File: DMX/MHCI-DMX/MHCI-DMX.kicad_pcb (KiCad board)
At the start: 2 copper layers, 100 x 100 mm, 36 parts, among them J1 XLR_Male, J2 XLR5_Female, J4 Barrel_Jack, K2 G5V-2, U2 TJA1051T, U4 74LVC1G08

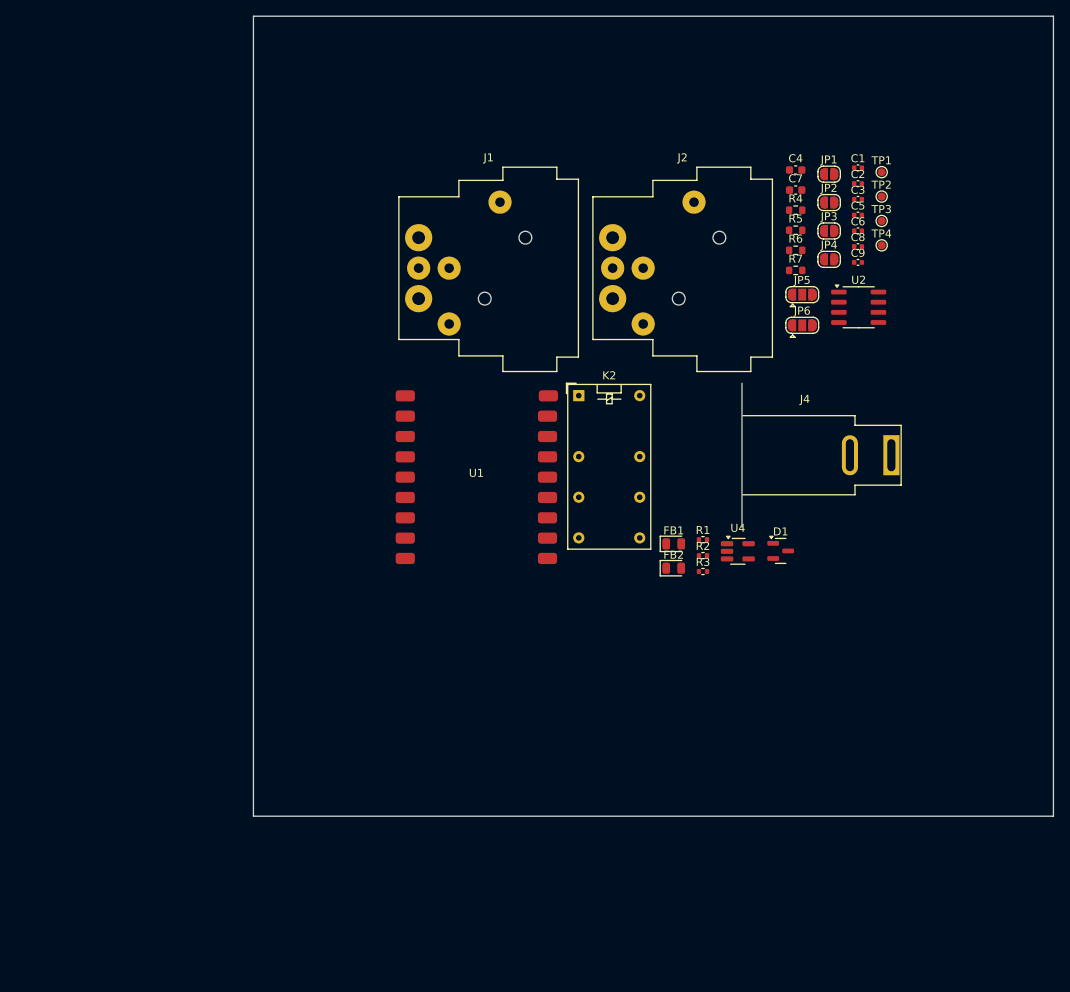
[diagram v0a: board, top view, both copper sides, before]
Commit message: DMX Schematic complete, and initial Layout
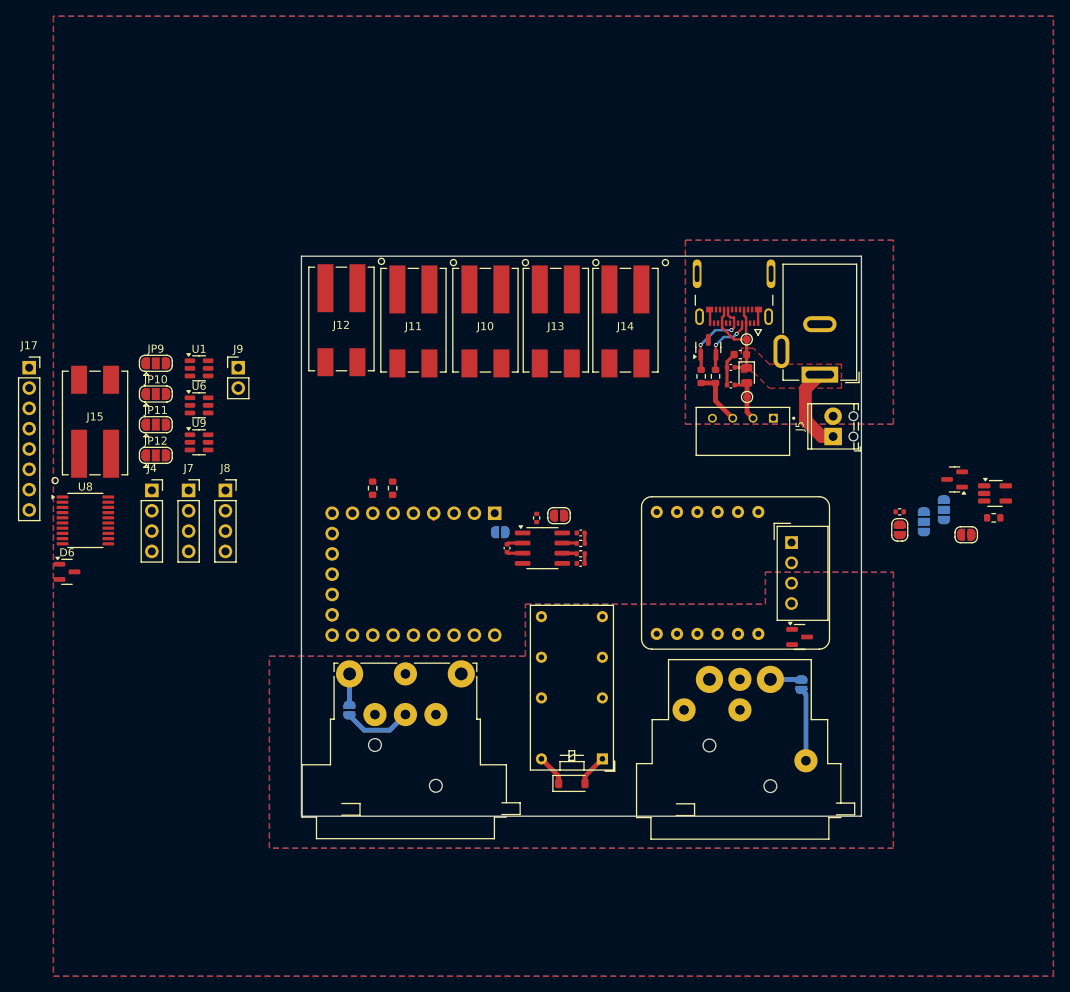
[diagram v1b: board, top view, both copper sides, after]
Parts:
- removed C7: 10uF, Capacitor_SMD:C_0603_1608Metric
- removed C8: 1uF, Capacitor_SMD:C_0402_1005Metric
- removed C9: 100nF, Capacitor_SMD:C_0402_1005Metric
- removed FB2: FerriteBead, Diode_SMD:D_0805_2012Metric
- removed TP3: VIN, TestPoint:TestPoint_Pad_D1.0mm
- removed TP4: 5V, TestPoint:TestPoint_Pad_D1.0mm
- added D2: D_TVS_Dual_AAC, Package_TO_SOT_SMD:SOT-23, F.Cu at (106.9, 91.4)
- added D4: D_TVS_Dual_AAC, Package_TO_SOT_SMD:SOT-23, F.Cu at (118.3, 127.6)
- added D6: D_TVS_Dual_AAC, Package_TO_SOT_SMD:SOT-23, F.Cu at (26.7, 119.5)
- added J10: Conn_01x02, MHCI:2060-452-998-404 Wago, F.Cu at (79.0, 88.0)
- added J11: Conn_01x02, MHCI:2060-452-998-404 Wago, F.Cu at (70.0, 88.0)
- added J12: Conn_01x02, MHCI:2060-452-998-404 Wago, F.Cu at (61.0, 87.8)
- added J13: Conn_01x02, MHCI:2060-452-998-404 Wago, F.Cu at (87.8, 88.0)
- added J14: Conn_01x02, MHCI:2060-452-998-404 Wago, F.Cu at (96.5, 88.0)
- added J15: Conn_01x02, MHCI:2060-452-998-404 Wago, F.Cu at (30.2, 100.9)
- added J17: Conn_01x08, Connector_PinSocket_2.54mm:PinSocket_1x08_P2.54mm_Vertical, F.Cu at (22.0, 93.9)
- added J3: 2012670005, LandingLight:MOLEX_2012670005, F.Cu at (110.1, 80.4)
- added J5: Conn_01x02, TerminalBlock_Phoenix:TerminalBlock_Phoenix_MPT-0,5-2-2.54_1x02_P2.54mm_Horizontal, F.Cu at (122.5, 102.5)
- added J6: Barrel_Jack_MountingPin, Connector_BarrelJack:BarrelJack_GCT_DCJ200-10-A_Horizontal, F.Cu at (120.8, 94.8)
- added J7: Conn_01x04, Connector_PinSocket_2.54mm:PinSocket_1x04_P2.54mm_Vertical, F.Cu at (41.9, 109.3)
- added J8: Conn_01x04, Connector_PinSocket_2.54mm:PinSocket_1x04_P2.54mm_Vertical, F.Cu at (46.5, 109.3)
- added J9: Conn_01x02, Connector_PinHeader_2.54mm:PinHeader_1x02_P2.54mm_Vertical, F.Cu at (48.1, 93.9)
- added JP10: SolderJumper_3_Open, Jumper:SolderJumper-3_P1.3mm_Open_RoundedPad1.0x1.5mm, F.Cu at (37.8, 97.2)
- added JP11: SolderJumper_3_Open, Jumper:SolderJumper-3_P1.3mm_Open_RoundedPad1.0x1.5mm, F.Cu at (37.8, 101.1)
- added JP12: SolderJumper_3_Open, Jumper:SolderJumper-3_P1.3mm_Open_RoundedPad1.0x1.5mm, F.Cu at (37.8, 104.9)
- added JP7: Jumper_2_Open, Jumper:SolderJumper-2_P1.3mm_Open_RoundedPad1.0x1.5mm, F.Cu at (139.1, 114.8)
- added JP8: Jumper_2_Open, Jumper:SolderJumper-2_P1.3mm_Open_RoundedPad1.0x1.5mm, F.Cu at (130.8, 114.2)
- added JP9: SolderJumper_3_Open, Jumper:SolderJumper-3_P1.3mm_Open_RoundedPad1.0x1.5mm, F.Cu at (37.8, 93.4)
- added PS1: TBA1-0510, MHCI:CONV_TBA1-0510, F.Cu at (111.2, 101.9)
- added Q1: PMOS, Package_TO_SOT_SMD:SOT-23, F.Cu at (137.6, 107.9)
- added R8: 100k, Resistor_SMD:R_0603_1608Metric, F.Cu at (142.5, 112.7)
- added R9: 120R, Resistor_SMD:R_0402_1005Metric, F.Cu at (130.8, 112.0)
- added U3: ~, MHCI:ISO-DMX, F.Cu at (113.1, 119.6)
- added U5: TME-0505S, Converter_DCDC:Converter_DCDC_TRACO_TME_03xxS_05xxS_12xxS_Single_THT, F.Cu at (117.3, 115.8)
- added U6: SRV05-4, Package_TO_SOT_SMD:SOT-23-6, F.Cu at (43.2, 98.6)
- added U7: ~, MHCI:ESP-32-S3-Tiny - PTH, F.Cu at (70.0, 119.8)
- added U8: TXB0108PW, Package_SO:TSSOP-20_4.4x6.5mm_P0.65mm, F.Cu at (29.0, 113.0)
- added U9: SRV05-4, Package_TO_SOT_SMD:SOT-23-6, F.Cu at (43.2, 103.3)
- D1: value D_TVS_Dual_AAC -> 1N4148W; footprint Package_TO_SOT_SMD:SOT-23 -> Diode_SMD:D_SOD-123
- J1: footprint Connector_Audio:Jack_XLR_Neutrik_NC5FAH-DA_Horizontal -> MHCI:Jack_XLR_Neutrik_NC5MAH_LR
- J2: footprint Connector_Audio:Jack_XLR_Neutrik_NC5FAH-0_Horizontal -> MHCI:Jack_XLR_Neutrik_NC5FAH_LR-DAE
- J4: value Barrel_Jack -> Conn_01x04; footprint Connector_BarrelJack:BarrelJack_SwitchcraftConxall_RAPC10U_Horizontal -> Connector_PinSocket_2.54mm:PinSocket_1x04_P2.54mm_Vertical
- JP1, JP3, JP4, JP5, JP6: moved to B.Cu
- U1: value ~ -> SRV05-4; footprint MHCI:ESP-32-S3-Zero - SMD -> Package_TO_SOT_SMD:SOT-23-6
- moved J4 92.5 mm to (37.3, 109.3)
- moved JP4 82.3 mm to (62.0, 136.8), turned to -90 degrees
- moved C1 64.7 mm to (81.7, 116.5), turned to 90 degrees
- moved R4 63.3 mm to (64.9, 109.0), turned to -90 degrees
- moved JP1 60.8 mm to (80.8, 114.5)
- moved R5 59.8 mm to (67.4, 109.0), turned to -90 degrees
- moved C2 58.8 mm to (90.9, 118.4)
- moved J2 58.6 mm to (114.6, 132.9), turned to -90 degrees
- moved JP3 56.8 mm to (118.5, 133.6), turned to -90 degrees
- moved J1 55.2 mm to (62.0, 132.2)
- moved C3 54.2 mm to (90.9, 114.6), turned to 180 degrees
- moved JP2 51.7 mm to (88.2, 112.4)
- moved U2 49.7 mm to (86.1, 116.5)
- moved K2 45.5 mm to (93.6, 142.8), turned to 180 degrees
- moved D1 39.1 mm to (89.8, 145.9)
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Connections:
- D1 pad 1: B -> +5V
- D1 pad 2: A -> /DMX_PASSTHROUGH
- J4 pad 1: VIN -> +5V
- J4 pad 2: Earth -> Net-(J4-Pin_2)
- K2 pad 1: unconnected-(K2-Pad1) -> /DMX_PASSTHROUGH
- K2 pad 16: Net-(K2-Pad16) -> +5V
- U1 pad 1: CAN_TX -> GPIO_X1_5
- U1 pad 2: CAN_RX -> GND
- U1 pad 3: SCL -> GPIO_X2_5
- U1 pad 4: SDA -> GPIO_X3_5
- U1 pad 5: /ESP_32_GPIO_05 -> +5V
- U1 pad 6: /ESP_32_GPIO_06 -> GPIO_X4_5
- U4 pad 2: unconnected-(U4-Pad2) -> DMX_EN
- U4 pad 4: Net-(K2-Pad16) -> Net-(Q1-G)
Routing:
- net VIN: track 0.00 -> 25.8 mm
- net +5V: track 0.00 -> 12.3 mm
- net /CC2: track 0.00 -> 11.0 mm, vias 0 -> 2
- net GND: track 0.00 -> 9.11 mm
- net Net-(JP3-B): track 0.00 -> 9.09 mm
- net Net-(JP4-B): track 0.00 -> 8.57 mm
- net /CC1: track 0.00 -> 7.92 mm, vias 0 -> 2
- net GND_DMX: track 0.00 -> 7.78 mm
- net Earth: track 0.00 -> 7.61 mm
- net /DMX_PASSTHROUGH: track 0.00 -> 3.97 mm
- net /CANH_L: track 0.00 -> 1.82 mm
- net /CANH_T: track 0.00 -> 1.82 mm
- net CANH: track 0.00 -> 1.32 mm
- net CANL: track 0.00 -> 1.21 mm
- net CAN_TX: track 0.00 -> 0.81 mm
- added copper zone on B.Cu, net Earth
- added copper zone on F.Cu, net Earth
- added copper zone on B.Cu, net GND
- added copper zone on F.Cu, net GND
- added copper zone on B.Cu, net GND_DMX
- added copper zone on F.Cu, net GND_DMX
- added copper zone on F.Cu, net VIN
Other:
- board size 100 x 100 mm -> 70 x 70 mm

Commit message: MHCI DMX - Finalise schematic and initial layout routing
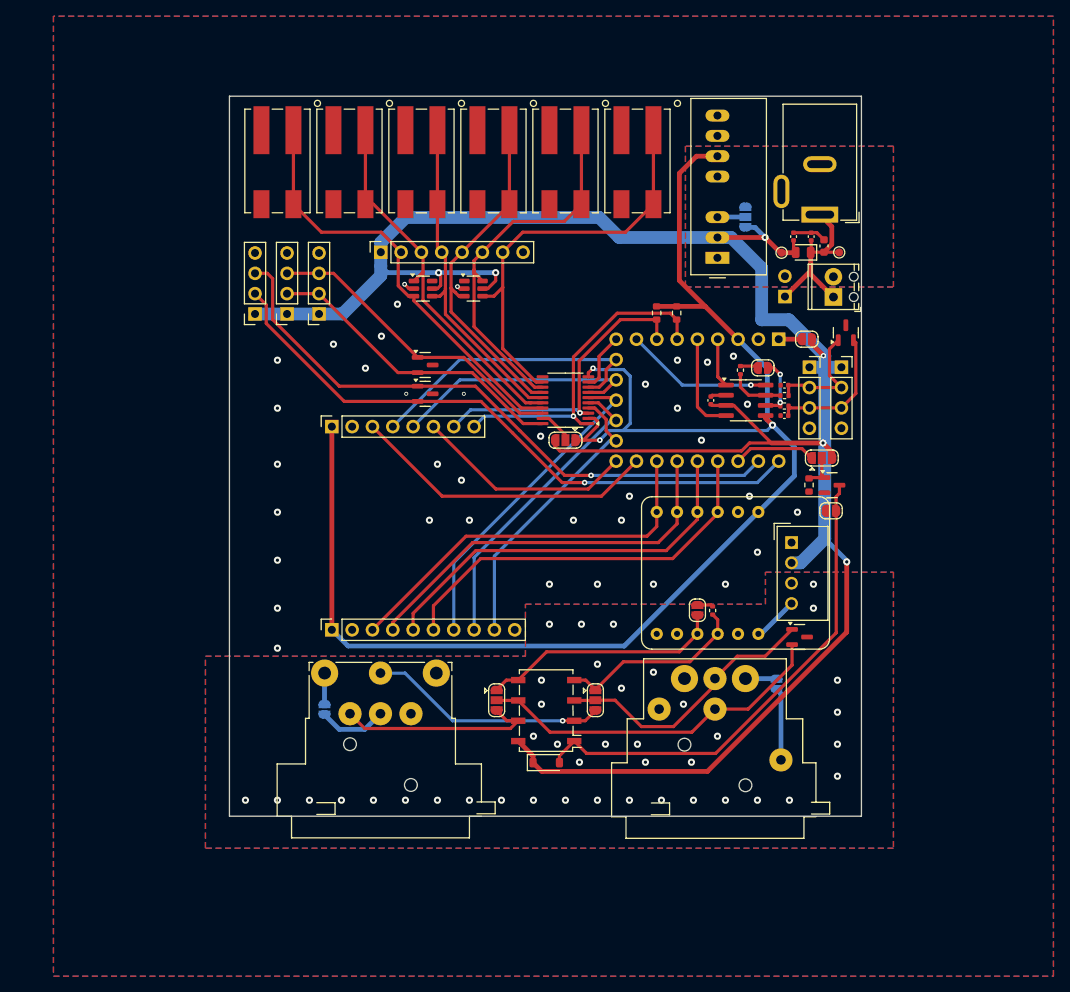
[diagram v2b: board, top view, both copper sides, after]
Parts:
- removed D2: D_TVS_Dual_AAC, Package_TO_SOT_SMD:SOT-23
- removed J3: 2012670005, LandingLight:MOLEX_2012670005
- removed JP10, JP11, JP12, JP9: SolderJumper_3_Open, Jumper:SolderJumper-3_P1.3mm_Open_RoundedPad1.0x1.5mm
- removed K2: G5V-2, Relay_THT:Relay_DPDT_Omron_G5V-2
- removed PS1: TBA1-0510, MHCI:CONV_TBA1-0510
- removed R6, R7: 5.1k, Resistor_SMD:R_0603_1608Metric
- removed U2: TJA1051T, Package_SO:SOIC-8_3.9x4.9mm_P1.27mm
- removed U6: SRV05-4, Package_TO_SOT_SMD:SOT-23-6
- added D3: D_TVS_Dual_AAC, Package_TO_SOT_SMD:SOT-23, F.Cu at (71.5, 93.6)
- added D5: D_TVS_Dual_AAC, Package_TO_SOT_SMD:SOT-23, F.Cu at (124.0, 89.6)
- added J16: Conn_01x04, Connector_PinSocket_2.54mm:PinSocket_1x04_P2.54mm_Vertical, F.Cu at (123.5, 93.9)
- added J18: Conn_01x04, Connector_PinSocket_2.54mm:PinSocket_1x04_P2.54mm_Vertical, F.Cu at (119.5, 93.9)
- added JP13: SolderJumper_3_Open, Jumper:SolderJumper-3_P1.3mm_Open_RoundedPad1.0x1.5mm, F.Cu at (121.0, 105.2)
- added JP14: SolderJumper_3_Open, Jumper:SolderJumper-3_P1.3mm_Open_RoundedPad1.0x1.5mm, B.Cu at (111.5, 75.1)
- added JP15: SolderJumper_3_Open, Jumper:SolderJumper-3_P1.3mm_Open_RoundedPad1.0x1.5mm, F.Cu at (89.0, 103.0)
- added K1: G6K-2, Relay_SMD:Relay_DPDT_Omron_G6K-2F, F.Cu at (86.6, 136.8)
- added U10: ~, MHCI:WirelessDMX-Module, F.Cu at (59.8, 114.0)
- added U11: TJA1051T-3, Package_SO:SOIC-8_3.9x4.9mm_P1.27mm, F.Cu at (111.5, 98.0)
- J9: moved to B.Cu
- JP1, JP5, JP6: moved to F.Cu
- U4: value 74LVC1G08 -> TEC2-1210WI; footprint Package_TO_SOT_SMD:SOT-23-5_HandSoldering -> Converter_DCDC:Converter_DCDC_TRACO_TMR-xxxx_THT
- moved J15 75.3 mm to (98.0, 68.1), turned to 180 degrees
- moved J9 68.9 mm to (116.4, 85.0)
- moved U8 61.9 mm to (89.0, 98.0), turned to 180 degrees
- moved JP6 57.9 mm to (80.4, 135.5), turned to -90 degrees
- moved D6 50.0 mm to (71.5, 97.2)
- moved JP5 49.6 mm to (92.7, 135.5), turned to -90 degrees
- moved J17 46.3 mm to (65.9, 79.5), turned to 90 degrees
- moved U4 45.5 mm to (108.0, 80.2), turned to 90 degrees
- moved JP1 45.3 mm to (119.2, 90.4)
- moved R4 41.7 mm to (100.4, 87.1)
- moved R5 41.7 mm to (102.9, 87.1)
- moved U7 41.6 mm to (105.5, 98.0)
- moved U9 39.3 mm to (77.5, 84.0)
- moved J10 32.7 mm to (53.0, 68.1)
- moved R2 31.5 mm to (116.4, 97.4)
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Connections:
- D6 pad 1: unconnected-(D6-A1-Pad1) -> UART_RX
- D6 pad 2: unconnected-(D6-A2-Pad2) -> UART_TX
- J4 pad 2: Net-(J4-Pin_2) -> SCL_5
- J4 pad 3: Net-(J4-Pin_3) -> SDA_5
- J7 pad 2: Net-(J7-Pin_2) -> SCL_5
- J7 pad 3: Net-(J7-Pin_3) -> SDA_5
- JP5 pad 1: /A_OUT -> A
- JP5 pad 2: A -> /A_OUT
- JP6 pad 1: /B_OUT -> B
- JP6 pad 2: B -> /B_OUT
- Q1 pad 1: Net-(Q1-G) -> Net-(JP13-C)
- R8 pad 1: Net-(Q1-G) -> Net-(JP13-C)
- U1 pad 1: GPIO_X1_5 -> GPIO_X2_5
- U1 pad 3: GPIO_X2_5 -> GPIO_X1_5
- U1 pad 6: GPIO_X4_5 -> unconnected-(U1-IO4-Pad6)
- U3 pad 1: +5V -> +3V3
- U4 pad 1: +5V -> Earth
- U4 pad 2: DMX_EN -> +5V
- U4 pad 3: GND -> Net-(JP14-C)
- U4 pad 5: +5V -> unconnected-(U4-NC-Pad5)
- U7 pad 10: GPIO_X6 -> GPIO_X2
- U7 pad 11: GPIO_X5 -> GPIO_X1
- U7 pad 12: /ESP_32_GPIO_12 -> I2C_nATTN
- U7 pad 13: /ESP_32_GPIO_13 -> SPI_nATTN
- U7 pad 6: GPIO_X1 -> GPIO_X6
- U7 pad 7: GPIO_X2 -> GPIO_X5
- U7 pad 8: GPIO_X3 -> CTI_RESET
- U7 pad 9: GPIO_X4 -> GPIO_X3
- U8 pad 10: unconnected-(U8-OE-Pad10) -> +3V3
- U8 pad 11: unconnected-(U8-GND-Pad11) -> GND
- U8 pad 19: unconnected-(U8-V_{CCB}-Pad19) -> Net-(JP15-C)
- U8 pad 2: unconnected-(U8-V_{CCA}-Pad2) -> +3V3
- U8 pad 7: GPIO_X4 -> CTI_RESET
- U9 pad 1: GPIO_X5_5 -> unconnected-(U9-IO1-Pad1)
- U9 pad 3: GPIO_X6_5 -> GPIO_X4_5
- U9 pad 4: UART_RX -> GPIO_X6_5
- U9 pad 6: UART_TX -> GPIO_X5_5
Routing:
- net +5V: track 12.3 -> 270.5 mm, vias 0 -> 6
- net +3V3: track 0.00 -> 193.3 mm, vias 0 -> 3
- net UART_TX: track 0.00 -> 77.7 mm, vias 0 -> 1
- net UART_RX: track 0.00 -> 77.1 mm, vias 0 -> 1
- net /DMX_PASSTHROUGH: track 3.97 -> 61.7 mm
- net GPIO_X1_5: track 0.00 -> 54.2 mm
- net GPIO_X6_5: track 0.00 -> 52.3 mm
- net R: track 0.00 -> 49.9 mm
- net NRE: track 0.00 -> 49.7 mm
- net DE: track 0.00 -> 49.4 mm
- net D: track 0.00 -> 49.1 mm
- net GPIO_X5_5: track 0.00 -> 47.4 mm
- net GPIO_X2_5: track 0.00 -> 46.9 mm
- net /B_OUT: track 0.00 -> 44.6 mm
- net GPIO_X4_5: track 0.00 -> 43.4 mm
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- removed copper zone on F.Cu, net VIN
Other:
- board size 70 x 70 mm -> 79 x 90 mm
- board text added: "TOOLING HOLES MOUNTING HOLES ROUNDED EDGES"

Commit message: Adding LEDs to DMX plug and socket.
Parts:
- added D10: GREEN, LED_SMD:LED_0603_1608Metric, F.Cu at (120.5, 149.0)
- added D7: RED, LED_SMD:LED_0603_1608Metric, F.Cu at (58.8, 149.1)
- added D8: GREEN, LED_SMD:LED_0603_1608Metric, F.Cu at (78.7, 149.0)
- added D9: RED, LED_SMD:LED_0603_1608Metric, F.Cu at (100.5, 149.1)
- added R10: 300R, Resistor_SMD:R_0603_1608Metric, F.Cu at (48.1, 117.9)
- added R11: 300R, Resistor_SMD:R_0603_1608Metric, F.Cu at (49.6, 117.9)
- added R12: 300R, Resistor_SMD:R_0603_1608Metric, F.Cu at (51.1, 117.9)
- added R13: 300R, Resistor_SMD:R_0603_1608Metric, F.Cu at (52.6, 117.9)
- added U2: ~, Package_SO:TSSOP-8_3x3mm_P0.65mm, F.Cu at (50.5, 113.2)
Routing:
- net +5V: track 270.5 -> 369.8 mm, vias 6 -> 10
- net Net-(D10-K): track 0.00 -> 90.6 mm
- net Net-(D9-K): track 0.00 -> 71.2 mm
- net Net-(D8-K): track 0.00 -> 50.9 mm
- net SCL: track 40.6 -> 77.0 mm
- net Net-(D7-K): track 0.00 -> 34.5 mm
- net SDA: track 38.6 -> 72.9 mm
- net +3V3: track 193.3 -> 211.3 mm, vias 3 -> 4
- net Net-(U2-LED0): track 0.00 -> 2.32 mm
- net Net-(U2-LED3): track 0.00 -> 2.19 mm
- net Net-(U2-LED1): track 0.00 -> 1.96 mm
- net Net-(U2-LED2): track 0.00 -> 1.84 mm
- net I2C_nATTN: track 27.5 -> 28.1 mm
- net GND_DMX: vias 41 -> 32
- net GND: vias 36 -> 42

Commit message: Logos and description
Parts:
- added H1: MountingHole, MountingHole:MountingHole_3.2mm_M3, F.Cu at (92.5, 82.5)
- added H2: MountingHole, MountingHole:MountingHole_3.2mm_M3, F.Cu at (122.5, 135.0)
- added H3: MountingHole, MountingHole:MountingHole_3.2mm_M3, F.Cu at (50.0, 95.0)
- added H4: MountingHole, MountingHole:MountingHole_3.2mm_M3, F.Cu at (50.0, 145.0)
- moved R10 6.02 mm to (48.2, 123.9)
- moved R11 6.02 mm to (49.7, 123.9)
- moved R12 6.02 mm to (51.2, 123.9)
- moved R13 6.02 mm to (52.7, 123.9)
- moved R9 3.84 mm to (103.6, 123.7)
- moved JP8 3.74 mm to (101.8, 123.7)
- moved JP1 0.38 mm to (119.1, 90.0)
- moved JP7 0.35 mm to (121.8, 111.8)
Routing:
- net Net-(D10-K): track 90.6 -> 83.9 mm
- net Net-(D9-K): track 71.2 -> 65.1 mm
- net Net-(D8-K): track 50.9 -> 44.8 mm
- net Net-(D7-K): track 34.5 -> 28.4 mm
- net Net-(U2-LED2): track 1.84 -> 7.90 mm
- net Net-(U2-LED3): track 2.19 -> 8.25 mm
- net Net-(U2-LED1): track 1.96 -> 7.94 mm
- net Net-(U2-LED0): track 2.32 -> 8.29 mm
- net A: track 24.0 -> 26.9 mm
- net B: track 30.3 -> 32.9 mm
- net +5V: track 369.8 -> 371.5 mm
- net GND_DMX: vias 32 -> 30
- net GND: vias 42 -> 64
- net (no net): vias 1 -> 0
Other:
- outline, holes or cut-outs redrawn
- board text added: "3V3"
- board text added: "5V"
- board text added: "5V ISO"
- board text added: "A"
- board text added: "B"
- board text added: "CAN 1"
- board text added: "CAN 2"
- board text added: "CAN Term"
- board text added: "CANH"
- board text added: "CANL"
- board text added: "CTI Reset"
- board text added: "D"
- board text added: "DE"
- board text added: "DMX"
- board text added: "DMX EN"
- board text added: "DMX ON"
- board text added: "DMX Plug"
- board text added: "DMX RS485 Module"
- board text added: "DMX Socket"
- board text added: "DMX Term"
- board text added: "ESP 5V"
- board text added: "ESP32"
- board text added: "GND"
- board text added: "GND ISO"
- board text added: "I2C"
- board text added: "I2C 1"
- board text added: "I2C 2"
- board text added: "IN"
- board text added: "INPUT"
- board text added: "IO1"
- board text added: "IO2"
- board text added: "IO3"
- board text added: "IO4"
- board text added: "IO5"
- board text added: "IO6"
- board text added: "LED 1"
- board text added: "LED 2"
- board text added: "LED 3"
- board text added: "LED 4"
- board text added: "LED Driver"
- board text added: "Logic Shifter"
- board text added: "MHCI DMX Dev Board v1.0"
- board text added: "MISO"
- board text added: "MOSI"
- board text added: "NRE"
- board text added: "OUT"
- board text added: "OUTPUT"
- board text added: "PSU EN"
- board text added: "R"
- board text added: "RX"
- board text added: "SCK"
- board text added: "SCL"
- board text added: "SDA"
- board text added: "SPI"
- board text added: "Shield"
- board text added: "TT"
- board text added: "TX"
- board text added: "UART"
- board text added: "VIN"
- board text added: "Wireless DMX Module"
- board text added: "nATTN"
- board text added: "nSS"
- board text removed: "TOOLING HOLES MOUNTING HOLES ROUNDED EDGES"
